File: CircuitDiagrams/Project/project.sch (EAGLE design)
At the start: 124 parts, among them IC1 UC3C, IC2 PCA9542A, IC3 MT48LC4M16A2TSOP54, IC4 TB6593FNGSSOP20, IC5 TB6593FNGSSOP20, J1 JTAG2.54MM2X5TH, J2 1BY2THROUGHHOLE, J3 1BY2THROUGHHOLE, J4 1BY2THROUGHHOLE, J5 8PIN2.54MM2X4TH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

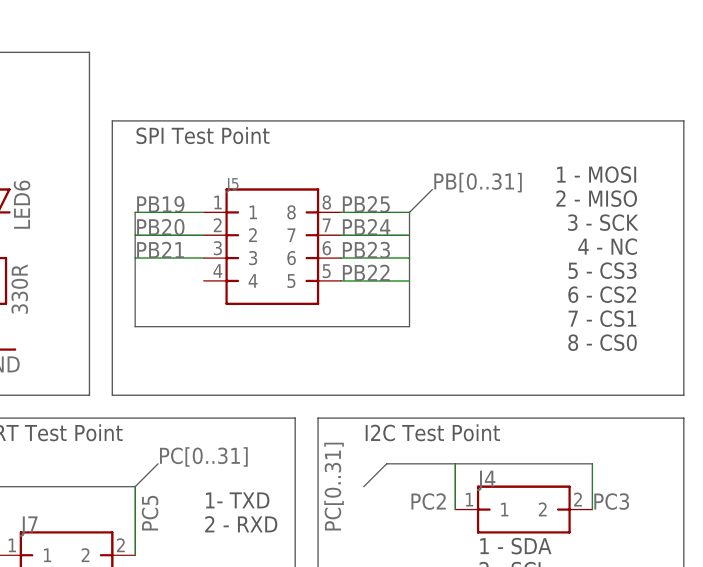
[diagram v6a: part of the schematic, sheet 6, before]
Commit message: Routed SPI and UART. Added GND to SPI Header
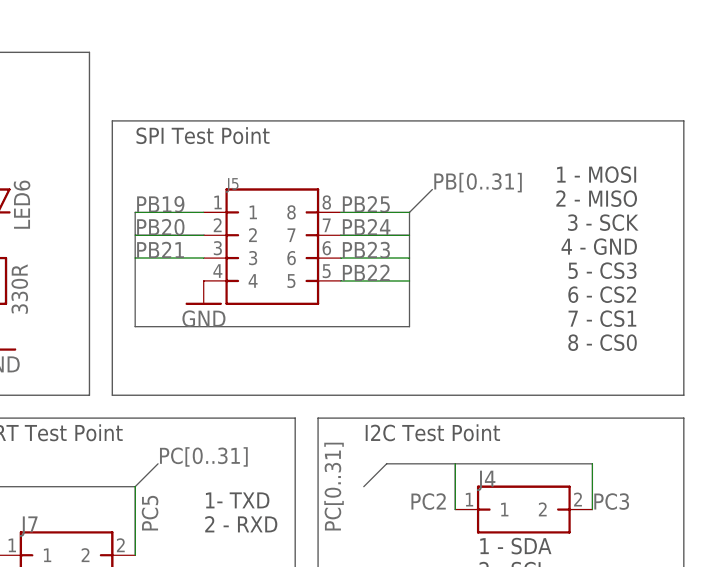
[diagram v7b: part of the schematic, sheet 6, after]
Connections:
- net GND: now also J5.4
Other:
- note added: "1 - MOSI 2 - MISO 3 - SCK 4 - GND 5 - CS3 6 - CS2 7 - CS1 8 - CS0"
- note removed: "1 - MOSI 2 - MISO 3 - SCK 4 - NC 5 - CS3 6 - CS2 7 - CS1 8 - CS0"
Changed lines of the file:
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@@
 <part name="+3V21" library="supply1" deviceset="+3V3" device=""/>
 <part name="J9" library="Headers" deviceset="16PIN" device="2.54MM2X8TH"/>
+<part name="GND47" library="supply1" deviceset="GND" device=""/>
 </parts>
 <sheets>
@@
 2 - MISO
 3 - SCK
-4 - NC
+4 - GND
 5 - CS3
 6 - CS2
@@
 <instance part="J8" gate="G$1" x="15.24" y="81.28" rot="R90"/>
 <instance part="J9" gate="G$1" x="33.02" y="81.28" rot="R90"/>
+<instance part="GND47" gate="1" x="78.74" y="33.02" rot="MR0"/>
 </instances>
 <busses>
@@
 <pinref part="GND45" gate="1" pin="GND"/>
 </segment>
+<segment>
+<pinref part="J5" gate="G$1" pin="4"/>
+<pinref part="GND47" gate="1" pin="GND"/>
+</segment>
 </net>

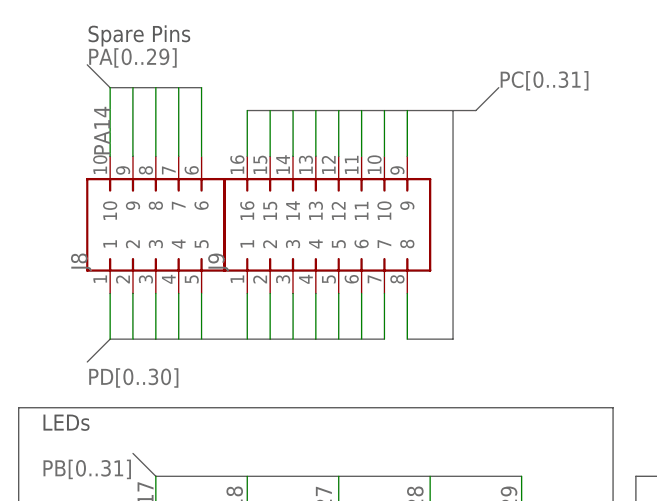
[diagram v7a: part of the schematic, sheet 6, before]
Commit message: Routed one motor driver and both sensors.
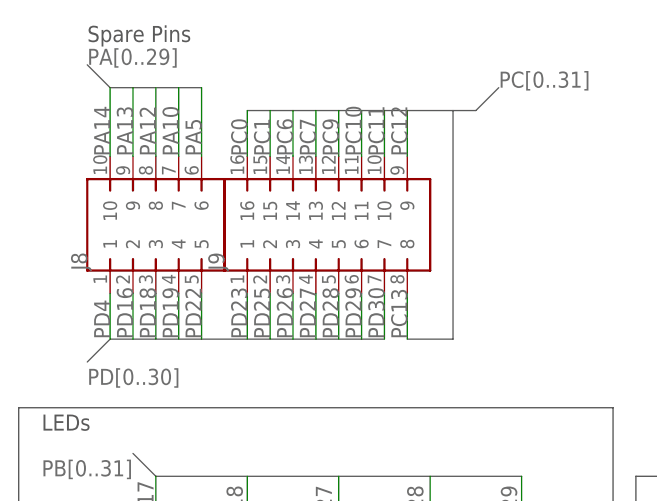
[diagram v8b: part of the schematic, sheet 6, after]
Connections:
- net N$1 renamed M21
- net N$2 renamed M22
- net N$3 renamed M12
- net N$4 renamed M11
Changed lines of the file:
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@@
 </segment>
 </net>
-<net name="N$1" class="0">
+<net name="M21" class="0">
 <segment>
 <pinref part="IC5" gate="G$1" pin="O1"/>
@@
 </segment>
 </net>
-<net name="N$2" class="0">
+<net name="M22" class="0">
 <segment>
 <pinref part="IC5" gate="G$1" pin="O2"/>
@@
 </segment>
 </net>
-<net name="N$3" class="0">
+<net name="M12" class="0">
 <segment>
 <pinref part="IC4" gate="G$1" pin="O2"/>
@@
 </segment>
 </net>
-<net name="N$4" class="0">
+<net name="M11" class="0">
 <segment>
 <pinref part="IC4" gate="G$1" pin="O1"/>
@@
 <pinref part="J8" gate="G$1" pin="6"/>
 <wire x1="20.32" y1="96.52" x2="20.32" y2="88.9" width="0.1524" layer="91"/>
+<label x="20.32" y="88.9" size="1.778" layer="95" rot="R90"/>
 </segment>
 </net>
@@
 <pinref part="J8" gate="G$1" pin="7"/>
 <wire x1="17.78" y1="88.9" x2="17.78" y2="96.52" width="0.1524" layer="91"/>
+<label x="17.78" y="88.9" size="1.778" layer="95" rot="R90"/>
 </segment>
 </net>
@@
 <pinref part="J8" gate="G$1" pin="8"/>
 <wire x1="15.24" y1="88.9" x2="15.24" y2="96.52" width="0.1524" layer="91"/>
+<label x="15.24" y="88.9" size="1.778" layer="95" rot="R90"/>
 </segment>
 </net>
@@
 <pinref part="J8" gate="G$1" pin="9"/>
 <wire x1="12.7" y1="88.9" x2="12.7" y2="96.52" width="0.1524" layer="91"/>
+<label x="12.7" y="88.9" size="1.778" layer="95" rot="R90"/>
 </segment>
 </net>
@@
 <pinref part="J9" gate="G$1" pin="16"/>
 <wire x1="25.4" y1="88.9" x2="25.4" y2="93.98" width="0.1524" layer="91"/>
+<label x="25.4" y="88.9" size="1.778" layer="95" rot="R90"/>
 </segment>
 </net>
@@
 <pinref part="J9" gate="G$1" pin="15"/>
 <wire x1="27.94" y1="88.9" x2="27.94" y2="93.98" width="0.1524" layer="91"/>
+<label x="27.94" y="88.9" size="1.778" layer="95" rot="R90"/>
 </segment>
 </net>
@@
 <pinref part="J9" gate="G$1" pin="14"/>
 <wire x1="30.48" y1="88.9" x2="30.48" y2="93.98" width="0.1524" layer="91"/>
+<label x="30.48" y="88.9" size="1.778" layer="95" rot="R90"/>
 </segment>
 </net>
@@
 <pinref part="J9" gate="G$1" pin="13"/>
 <wire x1="33.02" y1="88.9" x2="33.02" y2="93.98" width="0.1524" layer="91"/>
+<label x="33.02" y="88.9" size="1.778" layer="95" rot="R90"/>
 </segment>
 </net>
@@
 <pinref part="J9" gate="G$1" pin="12"/>
 <wire x1="35.56" y1="88.9" x2="35.56" y2="93.98" width="0.1524" layer="91"/>
+<label x="35.56" y="88.9" size="1.778" layer="95" rot="R90"/>
 </segment>
 </net>
@@
 <pinref part="J9" gate="G$1" pin="11"/>
 <wire x1="38.1" y1="88.9" x2="38.1" y2="93.98" width="0.1524" layer="91"/>
+<label x="38.1" y="88.9" size="1.778" layer="95" rot="R90"/>
 </segment>
 </net>
@@
 <pinref part="J9" gate="G$1" pin="10"/>
 <wire x1="40.64" y1="88.9" x2="40.64" y2="93.98" width="0.1524" layer="91"/>
+<label x="40.64" y="88.9" size="1.778" layer="95" rot="R90"/>
 </segment>
 </net>
@@
 <pinref part="J9" gate="G$1" pin="9"/>
 <wire x1="43.18" y1="88.9" x2="43.18" y2="93.98" width="0.1524" layer="91"/>
+<label x="43.18" y="88.9" size="1.778" layer="95" rot="R90"/>
 </segment>
 </net>
@@
 <pinref part="J9" gate="G$1" pin="8"/>
 <wire x1="43.18" y1="73.66" x2="43.18" y2="68.58" width="0.1524" layer="91"/>
+<label x="43.18" y="68.58" size="1.778" layer="95" rot="R90"/>
 </segment>
 </net>
@@
 <pinref part="J8" gate="G$1" pin="1"/>
 <wire x1="10.16" y1="73.66" x2="10.16" y2="68.58" width="0.1524" layer="91"/>
+<label x="10.16" y="68.58" size="1.778" layer="95" rot="R90"/>
 </segment>
 </net>
@@
 <pinref part="J8" gate="G$1" pin="2"/>
 <wire x1="12.7" y1="73.66" x2="12.7" y2="68.58" width="0.1524" layer="91"/>
+<label x="12.7" y="68.58" size="1.778" layer="95" rot="R90"/>
 </segment>
 </net>
@@
 <pinref part="J8" gate="G$1" pin="3"/>
 <wire x1="15.24" y1="73.66" x2="15.24" y2="68.58" width="0.1524" layer="91"/>
+<label x="15.24" y="68.58" size="1.778" layer="95" rot="R90"/>
 </segment>
 </net>
@@
 <pinref part="J8" gate="G$1" pin="4"/>
 <wire x1="17.78" y1="73.66" x2="17.78" y2="68.58" width="0.1524" layer="91"/>
+<label x="17.78" y="68.58" size="1.778" layer="95" rot="R90"/>
 </segment>
 </net>
@@
 <pinref part="J8" gate="G$1" pin="5"/>
 <wire x1="20.32" y1="73.66" x2="20.32" y2="68.58" width="0.1524" layer="91"/>
+<label x="20.32" y="68.58" size="1.778" layer="95" rot="R90"/>
 </segment>
 </net>
@@
 <pinref part="J9" gate="G$1" pin="1"/>
 <wire x1="25.4" y1="73.66" x2="25.4" y2="68.58" width="0.1524" layer="91"/>
+<label x="25.4" y="68.58" size="1.778" layer="95" rot="R90"/>
 </segment>
 </net>
@@
 <pinref part="J9" gate="G$1" pin="2"/>
 <wire x1="27.94" y1="73.66" x2="27.94" y2="68.58" width="0.1524" layer="91"/>
+<label x="27.94" y="68.58" size="1.778" layer="95" rot="R90"/>
 </segment>
 </net>
@@
 <pinref part="J9" gate="G$1" pin="3"/>
 <wire x1="30.48" y1="73.66" x2="30.48" y2="68.58" width="0.1524" layer="91"/>
+<label x="30.48" y="68.58" size="1.778" layer="95" rot="R90"/>
 </segment>
 </net>
@@
 <pinref part="J9" gate="G$1" pin="4"/>
 <wire x1="33.02" y1="73.66" x2="33.02" y2="68.58" width="0.1524" layer="91"/>
+<label x="33.02" y="68.58" size="1.778" layer="95" rot="R90"/>
 </segment>
 </net>
@@
 <pinref part="J9" gate="G$1" pin="5"/>
 <wire x1="35.56" y1="73.66" x2="35.56" y2="68.58" width="0.1524" layer="91"/>
+<label x="35.56" y="68.58" size="1.778" layer="95" rot="R90"/>
 </segment>
 </net>
@@
 <pinref part="J9" gate="G$1" pin="6"/>
 <wire x1="38.1" y1="73.66" x2="38.1" y2="68.58" width="0.1524" layer="91"/>
+<label x="38.1" y="68.58" size="1.778" layer="95" rot="R90"/>
 </segment>
 </net>
@@
 <pinref part="J9" gate="G$1" pin="7"/>
 <wire x1="40.64" y1="73.66" x2="40.64" y2="68.58" width="0.1524" layer="91"/>
-</segment>
-</net>
+<label x="40.64" y="68.58" size="1.778" layer="95" rot="R90"/>
+</segment>
+</net>
